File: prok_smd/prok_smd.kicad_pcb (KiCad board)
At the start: 2 copper layers, 105 x 41.2 mm, 60 parts, among them CON1 microSD_Card, J1 POWER, J10 Conn_01x02_Female, J11 Conn_01x02_Female, J12 Conn_01x05_Male, J13 Conn_01x02_Female, J14 Conn_01x02_Female, J15 Conn_01x02_Male, J16 Conn_01x02_Male, J17 Conn_01x02_Male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

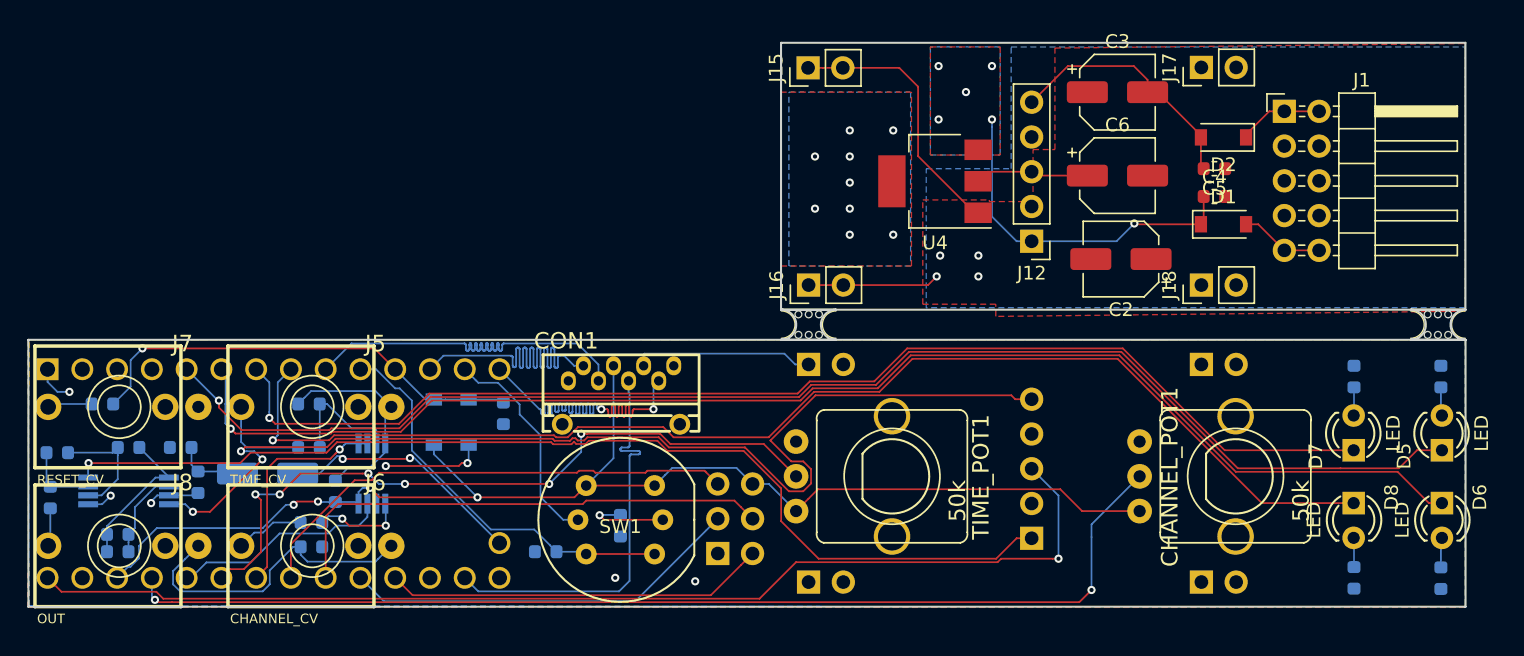
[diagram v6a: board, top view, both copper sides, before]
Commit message: :recycle: silkscreen cleanup
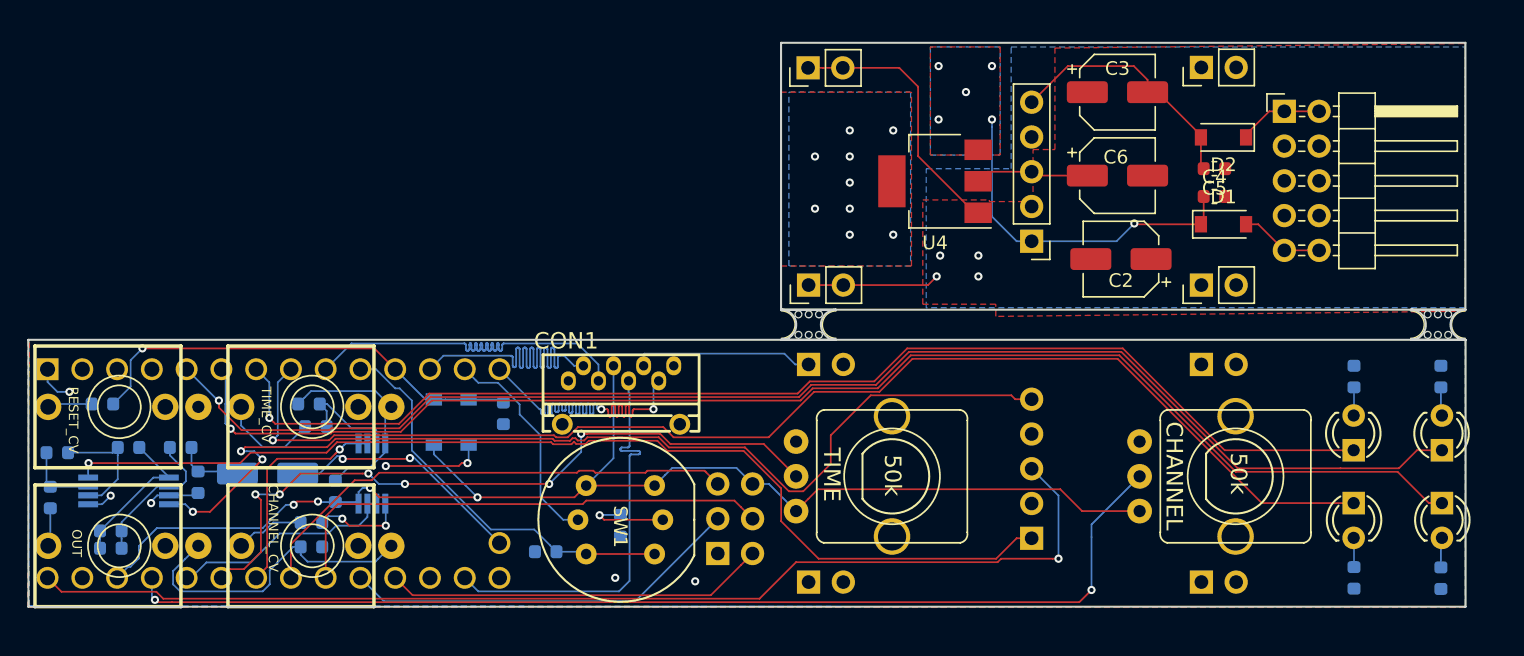
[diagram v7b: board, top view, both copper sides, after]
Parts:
- moved R6 1.61 mm to (121.0, 61.3)
- moved C8 0.57 mm to (106.0, 70.2)
- moved R3 0.57 mm to (106.0, 69.0)
- renumbered CHANNEL_POT1 to CHANNEL, J2 to EXPAND, TIME_POT1 to TIME
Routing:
- net -12V: track 98.7 -> 93.4 mm
- net Net-(C8-Pad1): track 6.56 -> 10.8 mm
- net TIME_CV: track 9.07 -> 7.76 mm

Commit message: :recycle: traces cleanup
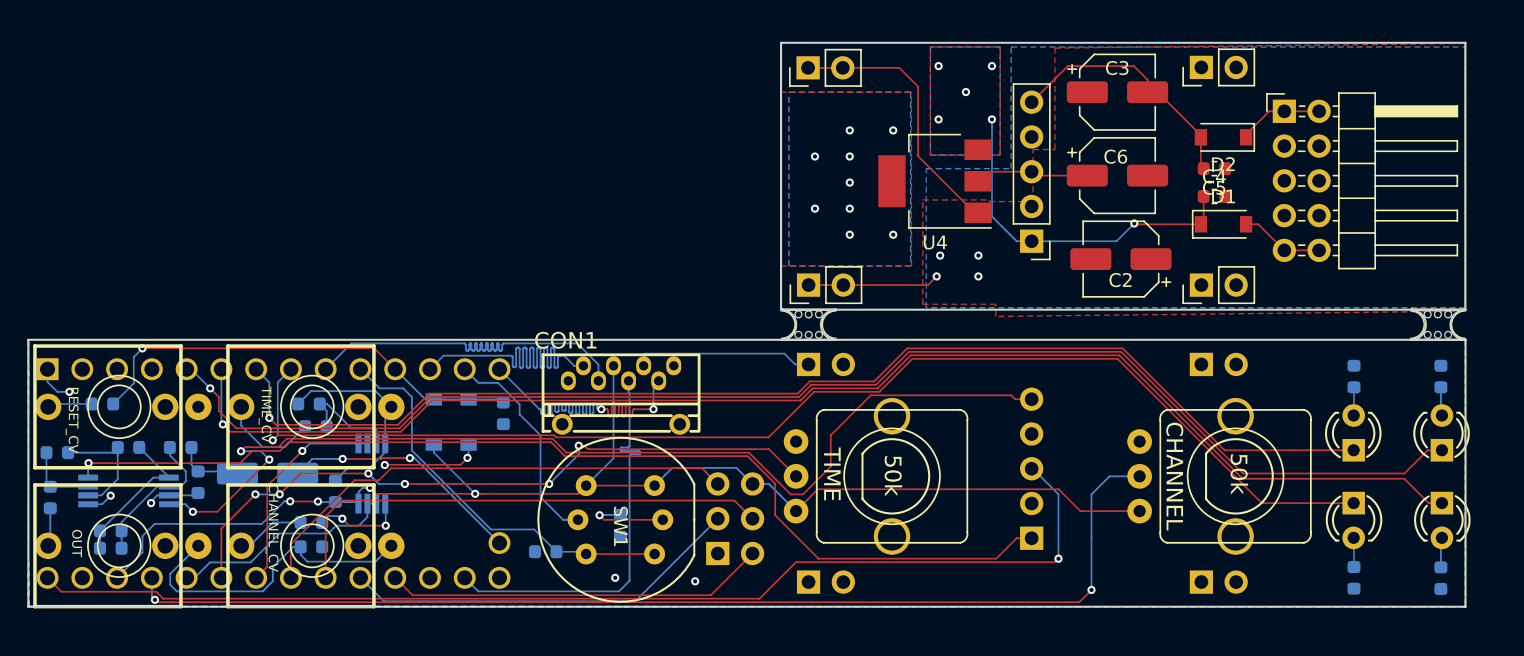
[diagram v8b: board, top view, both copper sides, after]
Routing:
- net TIME_POT: track 52.1 -> 50.0 mm
- net CHANNEL_POT: track 80.3 -> 81.6 mm
- net -12V: track 93.4 -> 94.3 mm
- net TIME_CV_ADC: track 16.4 -> 15.7 mm
- net LED_4: track 92.3 -> 91.7 mm
- net LED_1: track 100.3 -> 100.8 mm
